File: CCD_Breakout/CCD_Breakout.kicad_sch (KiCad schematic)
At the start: 8 parts, among them J1 Conn_01x03_Pin, U1 ILX511

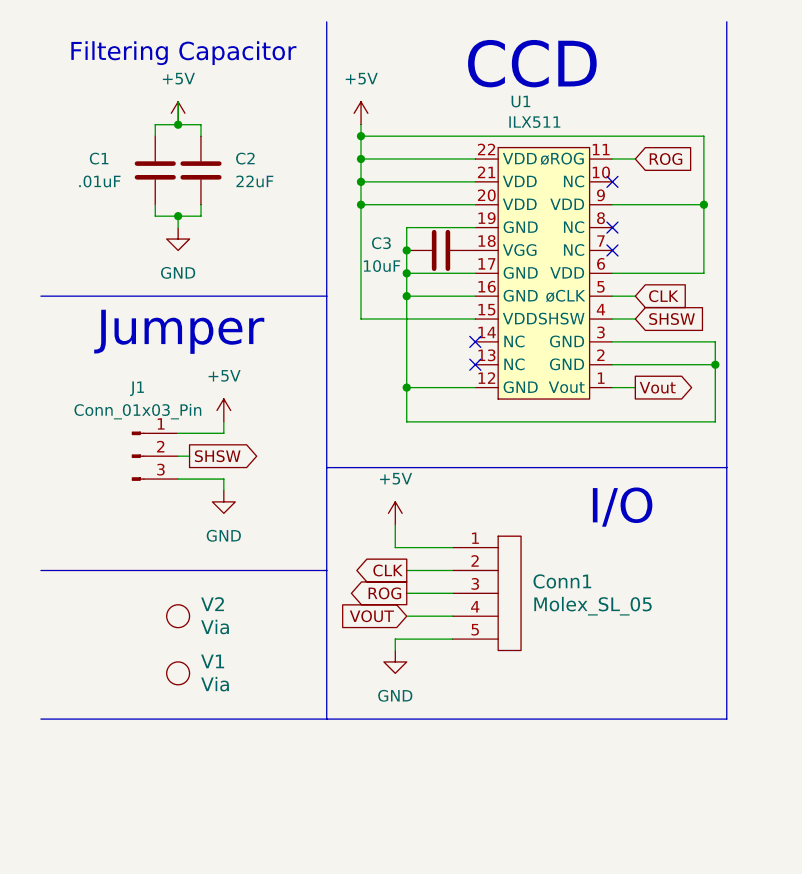
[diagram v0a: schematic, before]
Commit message: Added Mounting Holes
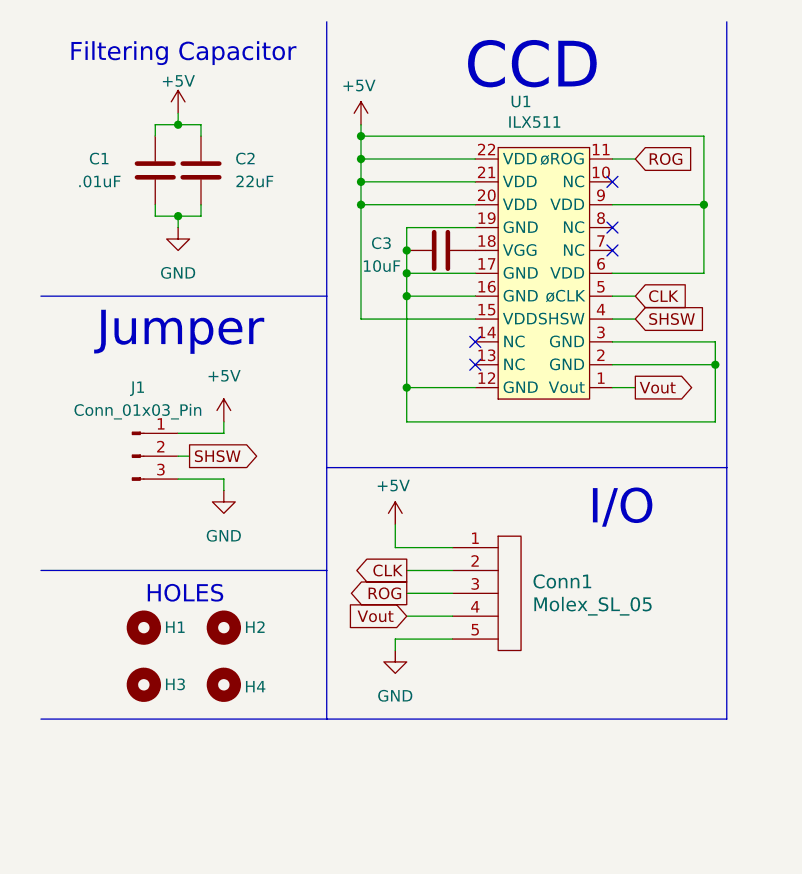
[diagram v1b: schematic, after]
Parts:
- removed V1, V2: Via, symbol MRDT_Drill_Holes:Via
- added H1, H2, H3, H4: ~, symbol Mechanical:MountingHole
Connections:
- net VOUT is gone; now on net Vout: Conn1.4
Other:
- note added: "HOLES"

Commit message: CCD GND
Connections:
- net GND: now also C3.1, U1.12 (GND), U1.16 (GND), U1.17 (GND), U1.19 (GND), U1.2 (GND), U1.3 (GND)
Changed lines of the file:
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@@
+	)
+	(junction
+		(at 74.93 46.99)
+		(diameter 0)
+		(color 0 0 0 0)
 	)
 	(junction
@@
 	)
 	(junction
-		(at 86.36 49.53)
+		(at 83.82 49.53)
 		(diameter 0)
 		(color 0 0 0 0)
 	)
 	(junction
-		(at 85.09 31.75)
+		(at 83.82 31.75)
 		(diameter 0)
 		(color 0 0 0 0)
@@
 		(color 0 0 0 0)
 	)
+	(junction
+		(at 83.82 55.88)
+		(diameter 0)
+		(color 0 0 0 0)
+	)
+	(junction
+		(at 74.93 49.53)
+		(diameter 0)
+		(color 0 0 0 0)
+	)
 	(no_connect
 		(at 59.69 49.53)
@@
 	(wire
 		(pts
-			(xy 74.93 31.75) (xy 85.09 31.75)
+			(xy 74.93 31.75) (xy 83.82 31.75)
 		)
 		(stroke
@@
 	(wire
 		(pts
+			(xy 83.82 55.88) (xy 83.82 57.15)
+		)
+		(stroke
+			(width 0)
+			(type default)
+		)
+	)
+	(wire
+		(pts
 			(xy 57.15 69.85) (xy 50.8 69.85)
 		)
@@
 	(wire
 		(pts
-			(xy 86.36 49.53) (xy 86.36 55.88)
+			(xy 83.82 49.53) (xy 83.82 55.88)
 		)
 		(stroke
@@
 	(wire
 		(pts
-			(xy 46.99 24.13) (xy 85.09 24.13)
+			(xy 46.99 24.13) (xy 83.82 24.13)
 		)
 		(stroke
@@
 		)
 	)
+	(wire
+		(pts
+			(xy 73.66 49.53) (xy 74.93 49.53)
+		)
+		(stroke
+			(width 0)
+			(type default)
+		)
+	)
 	(polyline
 		(pts
@@
 	(wire
 		(pts
-			(xy 74.93 46.99) (xy 86.36 46.99)
-		)
-		(stroke
-			(width 0)
-			(type default)
-		)
-	)
-	(wire
-		(pts
-			(xy 85.09 31.75) (xy 85.09 24.13)
+			(xy 83.82 31.75) (xy 83.82 24.13)
 		)
 		(stroke
@@
 	(wire
 		(pts
-			(xy 86.36 55.88) (xy 52.07 55.88)
+			(xy 83.82 55.88) (xy 52.07 55.88)
 		)
 		(stroke
@@
 	(wire
 		(pts
-			(xy 74.93 41.91) (xy 77.47 41.91)
+			(xy 74.93 46.99) (xy 83.82 46.99)
+		)
+		(stroke
+			(width 0)
+			(type default)
+		)
+	)
+	(wire
+		(pts
+			(xy 73.66 46.99) (xy 74.93 46.99)
+		)
+		(stroke
+			(width 0)
+			(type default)
+		)
+	)
+	(wire
+		(pts
+			(xy 74.93 41.91) (xy 76.2 41.91)
 		)
 		(stroke
@@
 	(wire
 		(pts
-			(xy 74.93 52.07) (xy 77.47 52.07)
-		)
-		(stroke
-			(width 0)
-			(type default)
-		)
-	)
-	(wire
-		(pts
-			(xy 86.36 49.53) (xy 74.93 49.53)
+			(xy 74.93 52.07) (xy 76.2 52.07)
+		)
+		(stroke
+			(width 0)
+			(type default)
+		)
+	)
+	(wire
+		(pts
+			(xy 83.82 49.53) (xy 74.93 49.53)
 		)
 		(stroke
@@
 	(wire
 		(pts
-			(xy 74.93 26.67) (xy 77.47 26.67)
+			(xy 74.93 26.67) (xy 76.2 26.67)
 		)
 		(stroke
@@
 	(wire
 		(pts
-			(xy 74.93 44.45) (xy 77.47 44.45)
+			(xy 74.93 44.45) (xy 76.2 44.45)
 		)
 		(stroke
@@
 	(wire
 		(pts
-			(xy 85.09 39.37) (xy 85.09 31.75)
-		)
-		(stroke
-			(width 0)
-			(type default)
-		)
-	)
-	(wire
-		(pts
-			(xy 74.93 39.37) (xy 85.09 39.37)
+			(xy 83.82 39.37) (xy 83.82 31.75)
+		)
+		(stroke
+			(width 0)
+			(type default)
+		)
+	)
+	(wire
+		(pts
+			(xy 74.93 39.37) (xy 83.82 39.37)
 		)
 		(stroke
@@
 	(wire
 		(pts
-			(xy 86.36 46.99) (xy 86.36 49.53)
+			(xy 83.82 46.99) (xy 83.82 49.53)
 		)
 		(stroke
@@
 	(global_label "CLK"
 		(shape input)
-		(at 77.47 41.91 0)
+		(at 76.2 41.91 0)
 		(fields_autoplaced yes)
 		(effects
@@
 		)
 		(property "Intersheetrefs" "${INTERSHEET_REFS}"
-			(at 84.0233 41.91 0)
+			(at 82.7533 41.91 0)
 			(effects
 				(font
@@
 	(global_label "ROG"
 		(shape input)
-		(at 77.47 26.67 0)
+		(at 76.2 26.67 0)
 		(fields_autoplaced yes)
 		(effects
@@
 		)
 		(property "Intersheetrefs" "${INTERSHEET_REFS}"
-			(at 84.3257 26.67 0)
+			(at 83.0557 26.67 0)
 			(effects
 				(font
@@
 	(global_label "SHSW"
 		(shape input)
-		(at 77.47 44.45 0)
+		(at 76.2 44.45 0)
 		(fields_autoplaced yes)
 		(effects
@@
 		)
 		(property "Intersheetrefs" "${INTERSHEET_REFS}"
-			(at 85.6561 44.45 0)
+			(at 84.3861 44.45 0)
 			(effects
 				(font
@@
 	(global_label "Vout"
 		(shape output)
-		(at 77.47 52.07 0)
+		(at 76.2 52.07 0)
 		(fields_autoplaced yes)
 		(effects
@@
 		)
 		(property "Intersheetrefs" "${INTERSHEET_REFS}"
-			(at 84.5675 52.07 0)
+			(at 83.2975 52.07 0)
 			(effects
 				(font
@@
 		)
 		(property "Value" "10uF"
-			(at 49.276 38.608 90)
+			(at 49.53 38.608 90)
 			(effects
 				(font
@@
 					(unit 1)
 				)
+			)
+		)
+	)
+	(symbol
+		(lib_id "power:GND")
+		(at 83.82 57.15 0)
+		(unit 1)
+		(exclude_from_sim no)
+		(in_bom yes)
+		(on_board yes)
+		(dnp no)
+		(property "Reference" "#PWR08"
+			(at 83.82 63.5 0)
+			(effects
+				(font
+					(size 1.27 1.27)
+				)
+				(hide yes)
+			)
+		)
+		(property "Value" "GND"
+			(at 79.502 58.928 0)
+			(effects
+				(font
+					(size 1.27 1.27)
+				)
+			)
+		)
+		(property "Footprint" ""
+			(at 83.82 57.15 0)
+			(effects
+				(font
+					(size 1.27 1.27)
+				)
+				(hide yes)
+			)
+		)
+		(property "Datasheet" ""
+			(at 83.82 57.15 0)
+			(effects
+				(font
+					(size 1.27 1.27)
+				)
+				(hide yes)
+			)
+		)
+		(property "Description" "Power symbol creates a global label with name \"GND\" , ground"
+			(at 83.82 57.15 0)
+			(effects
+				(font
+					(size 1.27 1.27)
+				)
+				(hide yes)
+			)
+		)
+		(pin "1"
+		)
+		(instances
+			(project "CCD_Breakout"
+				(path "/8c44394f-ce06-4603-9f88-0202e05c26c7"
+					(reference "#PWR08")
+					(unit 1)
+				)

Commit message: Updates
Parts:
- removed J1: Conn_01x03_Pin, symbol Connector:Conn_01x03_Pin
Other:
- note removed: "Jumper"
- moved on the sheet: H1, H2, H3, H4

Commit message: updated schematic
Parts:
- added Q1: PNP, symbol Simulation_SPICE:PNP
- added R1: 3k, symbol Device:R
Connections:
- net +5V: now also R1.1
- net GND: now also Q1.1 (C)
- net Vout: now also Q1.3 (E), R1.2; no longer U1.1 (Vout)
- new net: Q1.2 (B), U1.1 (Vout)
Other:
- moved on the sheet: Conn1, U1

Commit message: Started on CCD
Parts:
- C1, C2, C3: footprint (none) -> Capacitor_SMD:C_0603_1608Metric_Pad1.08x0.95mm_HandSolder
- Conn1: footprint (none) -> MRDT_Connectors:MOLEX_SL_05_Vertical
- H1, H2, H3, H4: footprint (none) -> MRDT_Drill_Holes:4_40_Hole
- Q1: footprint (none) -> Package_TO_SOT_SMD:SOT-23
- R1: footprint (none) -> Resistor_SMD:R_0603_1608Metric_Pad0.98x0.95mm_HandSolder
- U1: footprint (none) -> MRDT_CCD:ILX511
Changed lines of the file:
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@@
 			)
 		)
-		(property "Footprint" ""
+		(property "Footprint" "MRDT_CCD:ILX511"
 			(at 76.2 40.64 0)
 			(effects
@@
 			)
 		)
-		(property "Footprint" ""
+		(property "Footprint" "Capacitor_SMD:C_0603_1608Metric_Pad1.08x0.95mm_HandSolder"
 			(at 30.1752 31.75 0)
 			(effects
@@
 			)
 		)
-		(property "Footprint" ""
+		(property "Footprint" "Capacitor_SMD:C_0603_1608Metric_Pad1.08x0.95mm_HandSolder"
 			(at 25.0952 31.75 0)
 			(effects
@@
 			)
 		)
-		(property "Footprint" ""
+		(property "Footprint" "MRDT_Drill_Holes:4_40_Hole"
 			(at 30.48 48.26 0)
 			(effects
@@
 			)
 		)
-		(property "Footprint" ""
+		(property "Footprint" "Resistor_SMD:R_0603_1608Metric_Pad0.98x0.95mm_HandSolder"
 			(at 66.04 64.008 90)
 			(effects
@@
 			)
 		)
-		(property "Footprint" ""
+		(property "Footprint" "MRDT_Connectors:MOLEX_SL_05_Vertical"
 			(at 62.23 95.25 0)
 			(effects
@@
 			)
 		)
-		(property "Footprint" ""
+		(property "Footprint" "MRDT_Drill_Holes:4_40_Hole"
 			(at 30.48 54.61 0)
 			(effects
@@
 			)
 		)
-		(property "Footprint" ""
+		(property "Footprint" "Capacitor_SMD:C_0603_1608Metric_Pad1.08x0.95mm_HandSolder"
 			(at 59.69 35.8648 0)
 			(effects
@@
 			)
 		)
-		(property "Footprint" ""
+		(property "Footprint" "MRDT_Drill_Holes:4_40_Hole"
 			(at 21.59 54.61 0)
 			(effects
@@
 			)
 		)
-		(property "Footprint" ""
+		(property "Footprint" "Package_TO_SOT_SMD:SOT-23"
 			(at 77.47 95.25 0)
 			(effects
@@
 			)
 		)
-		(property "Footprint" ""
+		(property "Footprint" "MRDT_Drill_Holes:4_40_Hole"
 			(at 21.59 48.26 0)
 			(effects

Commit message: Updated CCD
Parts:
- removed H3, H4: ~, MRDT_Drill_Holes:4_40_Hole, symbol Mechanical:MountingHole
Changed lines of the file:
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@@
 	(polyline
 		(pts
-			(xy 11.43 58.42) (xy 43.18 58.42)
+			(xy 11.43 53.34) (xy 43.18 53.34)
 		)
 		(stroke
@@
 	)
 	(symbol
-		(lib_id "Mechanical:MountingHole")
-		(at 30.48 54.61 0)
-		(unit 1)
-		(exclude_from_sim yes)
-		(in_bom no)
-		(on_board yes)
-		(dnp no)
-		(property "Reference" "H4"
-			(at 32.766 54.864 0)
-			(effects
-				(font
-					(size 1.27 1.27)
-				)
-				(justify left)
-			)
-		)
-		(property "Value" "~"
-			(at 33.02 55.88 0)
-			(effects
-				(font
-					(size 1.27 1.27)
-				)
-				(justify left)
-			)
-		)
-		(property "Footprint" "MRDT_Drill_Holes:4_40_Hole"
-			(at 30.48 54.61 0)
-			(effects
-				(font
-					(size 1.27 1.27)
-				)
-				(hide yes)
-			)
-		)
-		(property "Datasheet" "~"
-			(at 30.48 54.61 0)
-			(effects
-				(font
-					(size 1.27 1.27)
-				)
-				(hide yes)
-			)
-		)
-		(property "Description" "Mounting Hole without connection"
-			(at 30.48 54.61 0)
-			(effects
-				(font
-					(size 1.27 1.27)
-				)
-				(hide yes)
-			)
-		)
-		(instances
-			(project "CCD_Breakout"
-				(path "/8c44394f-ce06-4603-9f88-0202e05c26c7"
-					(reference "H4")
-					(unit 1)
-				)
-			)
-		)
-	)
-	(symbol
 		(lib_id "power:GND")
 		(at 26.67 34.29 0)
@@
 					(unit 1)
 				)
-			)
-		)
-	)
-	(symbol
-		(lib_id "Mechanical:MountingHole")
-		(at 21.59 54.61 0)
-		(unit 1)
-		(exclude_from_sim yes)
-		(in_bom no)
-		(on_board yes)
-		(dnp no)
-		(property "Reference" "H3"
-			(at 23.876 54.61 0)
-			(effects
-				(font
-					(size 1.27 1.27)
-				)
-				(justify left)
-			)
-		)
-		(property "Value" "~"
-			(at 24.13 55.88 0)
-			(effects
-				(font
-					(size 1.27 1.27)
-				)
-				(justify left)
-			)
-		)
-		(property "Footprint" "MRDT_Drill_Holes:4_40_Hole"
-			(at 21.59 54.61 0)
-			(effects
-				(font
-					(size 1.27 1.27)
-				)
-				(hide yes)
-			)
-		)
-		(property "Datasheet" "~"
-			(at 21.59 54.61 0)
-			(effects
-				(font
-					(size 1.27 1.27)
-				)
-				(hide yes)
-			)
-		)
-		(property "Description" "Mounting Hole without connection"
-			(at 21.59 54.61 0)
-			(effects
-				(font
-					(size 1.27 1.27)
-				)
-				(hide yes)
-			)
-		)
-		(instances
-			(project "CCD_Breakout"
-				(path "/8c44394f-ce06-4603-9f88-0202e05c26c7"
-					(reference "H3")
-					(unit 1)
-				)

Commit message: CCD Changes
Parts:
- removed C1: .01uF, Capacitor_SMD:C_0603_1608Metric_Pad1.08x0.95mm_HandSolder, symbol Device:C
- removed C2: 22uF, Capacitor_SMD:C_0603_1608Metric_Pad1.08x0.95mm_HandSolder, symbol Device:C
- removed C3: 10uF, Capacitor_SMD:C_0603_1608Metric_Pad1.08x0.95mm_HandSolder, symbol Device:C
- removed Conn1: Molex_SL_05, MRDT_Connectors:MOLEX_SL_05_Vertical, symbol MRDT_Connectors:Molex_SL_05
- removed H1, H2: ~, MRDT_Drill_Holes:4_40_Hole, symbol Mechanical:MountingHole
- removed Q1: PNP, Package_TO_SOT_SMD:SOT-23, symbol Simulation_SPICE:PNP
- removed R1: 3k, Resistor_SMD:R_0603_1608Metric_Pad0.98x0.95mm_HandSolder, symbol Device:R
- removed U1: ILX511, MRDT_CCD:ILX511, symbol MRDT_CCD:ILX511
- added C4: .01uF, Capacitor_SMD:C_0603_1608Metric_Pad1.08x0.95mm_HandSolder, symbol Device:C
- added C5: 22uF, Capacitor_SMD:C_0603_1608Metric_Pad1.08x0.95mm_HandSolder, symbol Device:C
- added C6: 10uF, Capacitor_SMD:C_0603_1608Metric_Pad1.08x0.95mm_HandSolder, symbol Device:C
- added Conn2: Molex_SL_05, MRDT_Connectors:MOLEX_SL_05_Vertical, symbol MRDT_Connectors:Molex_SL_05
- added H3, H4: ~, MRDT_Drill_Holes:4_40_Hole, symbol Mechanical:MountingHole
- added Q2: PNP, Package_TO_SOT_SMD:SOT-23, symbol Simulation_SPICE:PNP
- added R2: 3k, Resistor_SMD:R_0603_1608Metric_Pad0.98x0.95mm_HandSolder, symbol Device:R
- added U2: ILX511, MRDT_CCD:ILX511, symbol MRDT_CCD:ILX511
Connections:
- net +5V: now also C4.1, C5.1, Conn2.1, R2.1, U2.15 (VDD), U2.20 (VDD), U2.21 (VDD), U2.22 (VDD), U2.6 (VDD), U2.9 (VDD)
- net CLK: now also Conn2.2, U2.5 (øCLK)
- net GND: now also C4.2, C5.2, C6.1, Conn2.5, Q2.1 (C), U2.12 (GND), U2.16 (GND), U2.17 (GND), U2.19 (GND), U2.2 (GND), U2.3 (GND)
- net ROG: now also Conn2.3, U2.11 (øROG)
- net SHSW: now also U2.4 (SHSW)
- net Vout: now also Conn2.4, Q2.3 (E), R2.2
- new net: Q2.2 (B), U2.1 (Vout)
- new net: C6.2, U2.18 (VGG)

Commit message: cat
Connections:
- net CLK: now also Conn2.4; no longer Conn2.2
- net Vout: now also Conn2.2; no longer Conn2.4
